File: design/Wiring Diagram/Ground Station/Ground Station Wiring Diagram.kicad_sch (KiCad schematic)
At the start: 4 parts, among them U1 KY-023, U2 NRF24L01, U3 KY-023

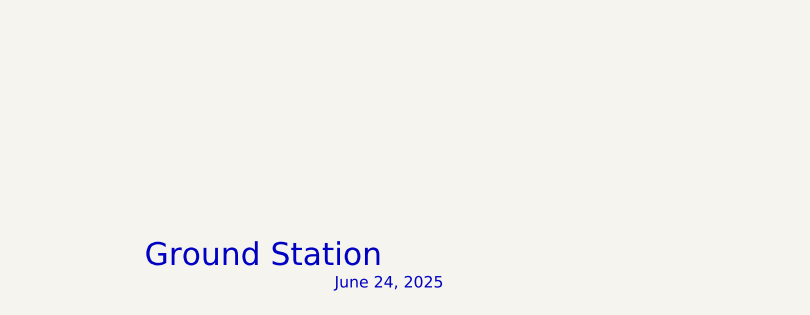
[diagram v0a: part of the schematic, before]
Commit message: Add wiring diagrams svg.
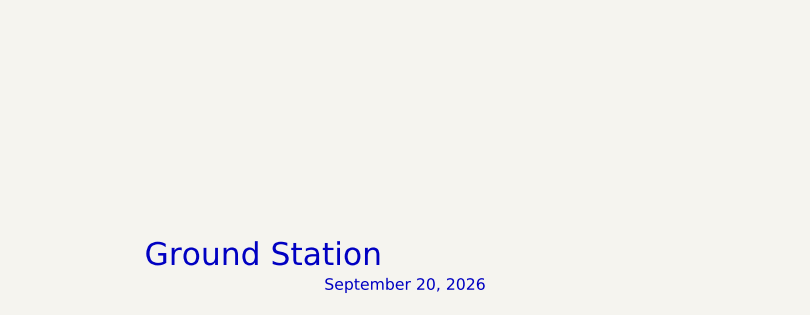
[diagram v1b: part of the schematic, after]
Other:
- note added: "September 20, 2026"
- note removed: "June 24, 2025"
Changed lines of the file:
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@@
 		)
 	)
-	(text "June 24, 2025\n"
+	(text "September 20, 2026\n"
 		(exclude_from_sim no)
-		(at 214.63 193.04 0)
+		(at 216.408 193.294 0)
 		(effects
 			(font
